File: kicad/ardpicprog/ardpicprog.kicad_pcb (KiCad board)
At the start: 2 copper layers, 69.2 x 53.9 mm, 37 parts, among them P1 CONN_01X06, P2 CONN_01X02, Q1 BC548, SW1 SW_PUSH, U1 PIC16F627, U2 MC34063, U3 LM78L12ACZ

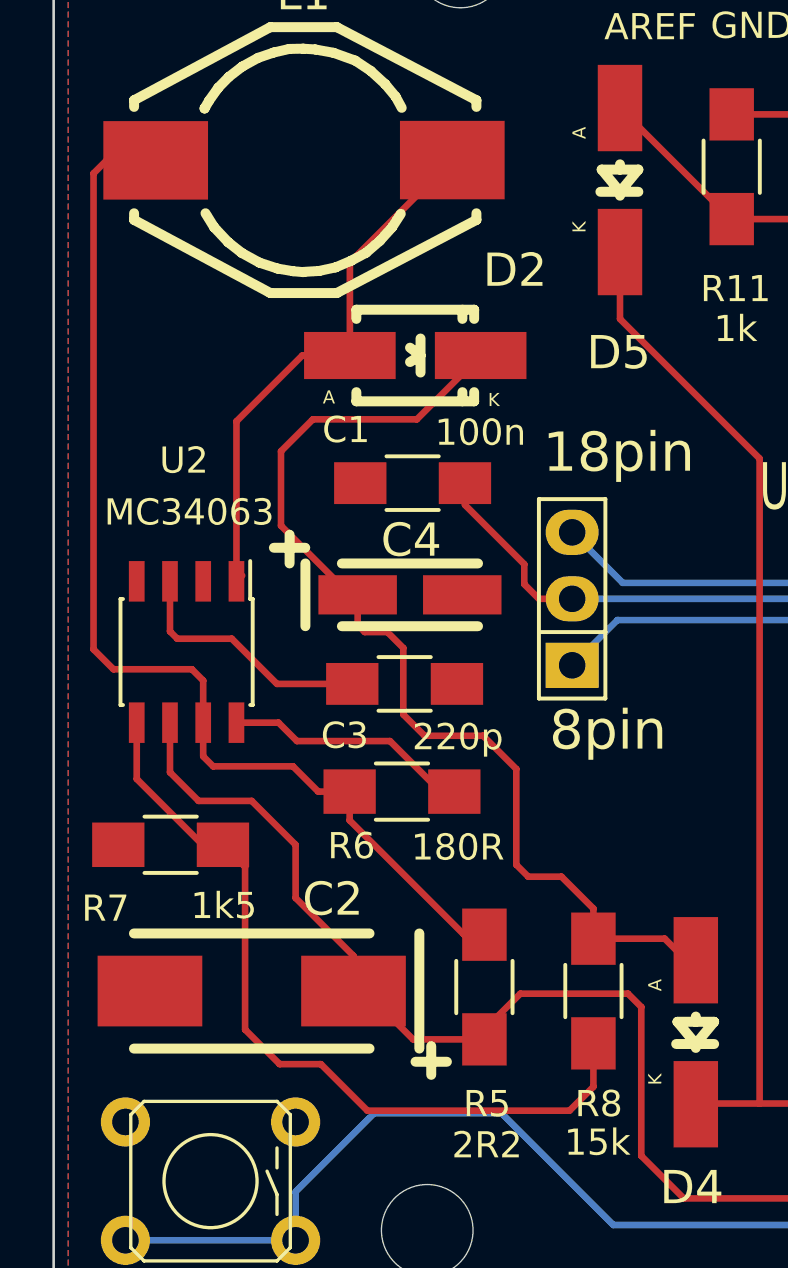
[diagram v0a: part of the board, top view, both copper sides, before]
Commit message: update c2 to 10u/6.3V on 5V line
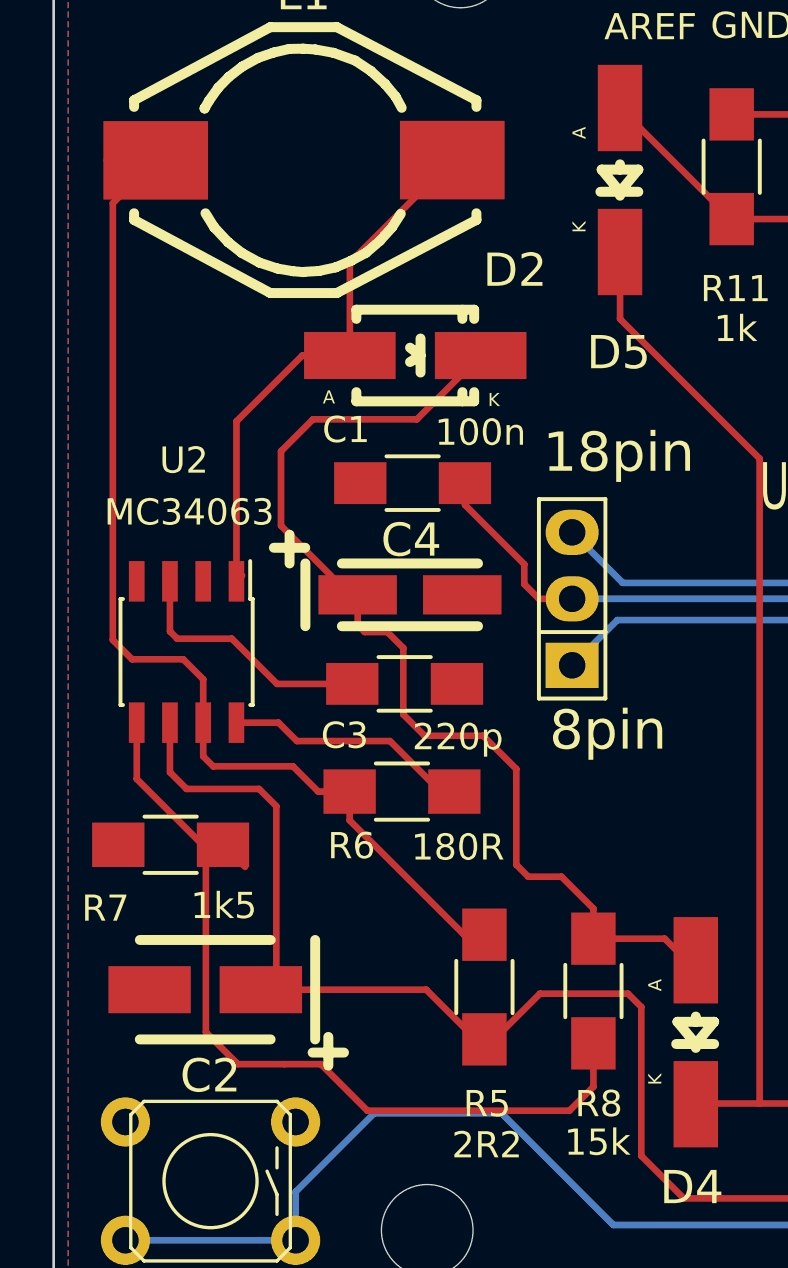
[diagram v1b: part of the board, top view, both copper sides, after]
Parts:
- C2: value 10m/35V -> 10m/6,3V; footprint Capacitors_Tantalum_SMD:TantalC_SizeD_EIA-7343_HandSoldering -> Capacitors_Tantalum_SMD:TantalC_SizeB_EIA-3528_HandSoldering
- moved C2 1.78 mm to (135.1, 118.3)
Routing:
- net 5V: track 51.9 -> 55.0 mm
- net Net-(R7-Pad1): track 30.5 -> 33.2 mm
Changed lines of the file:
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@@
     (links 73)
     (no_connects 0)
-    (area 117.87777 70.9168 221.46623 133.98246)
+    (area 129.286799 76.099199 198.576401 130.148801)
     (thickness 1.6)
     (drawings 34)
-    (tracks 232)
+    (tracks 234)
     (zones 0)
     (modules 37)
@@
       (outputformat 1)
       (mirror false)
-      (drillshape 1)
+      (drillshape 0)
       (scaleselection 1)
       (outputdirectory ""))
@@
     )
   )
-  (module Capacitors_Tantalum_SMD:TantalC_SizeD_EIA-7343_HandSoldering (layer F.Cu)
-    (at 136.906 118.364 180)
-    (descr "Tantal Cap. , Size D, EIA-7343, Hand Soldering,")
-    (tags "Tantal Cap. , Size D, EIA-7343, Hand Soldering,")
-    (attr smd)
-    (fp_text reference C2 (at -3.0988 3.5052 180) (layer F.SilkS)
-      (effects (font (thickness 0.3048)))
-    )
-    (fp_text value 10m/35V (at -0.09906 3.59918 180) (layer F.SilkS) hide
-      (effects (font (thickness 0.3048)))
-    )
-    (fp_line (start -6.40334 -2.19964) (end -6.40334 2.19964) (layer F.SilkS) (width 0.381))
-    (fp_line (start -4.50088 2.19964) (end 4.50088 2.19964) (layer F.SilkS) (width 0.381))
-    (fp_line (start 4.50088 -2.19964) (end -4.50088 -2.19964) (layer F.SilkS) (width 0.381))
-    (fp_text user + (at -6.85546 -2.70002 180) (layer F.SilkS)
-      (effects (font (thickness 0.3048)))
-    )
-    (fp_line (start -6.858 -3.20294) (end -6.858 -2.10312) (layer F.SilkS) (width 0.381))
-    (fp_line (start -7.45744 -2.70256) (end -6.25856 -2.70256) (layer F.SilkS) (width 0.381))
-    (pad 2 smd rect (at 3.88874 0 180) (size 4.0005 2.70002) (layers F.Cu F.Paste F.Mask)
-      (net 2 GND))
-    (pad 1 smd rect (at -3.88874 0 180) (size 4.0005 2.70002) (layers F.Cu F.Paste F.Mask)
-      (net 3 5V))
-  )
   (module Capacitors_SMD:C_1206_HandSoldering (layer F.Cu)
     (at 142.748 106.6292)
@@
     (pad 1 thru_hole circle (at 0 0) (size 3.50012 3.50012) (drill 3.50012) (layers))
   )
+  (module Capacitors_Tantalum_SMD:TantalC_SizeB_EIA-3528_HandSoldering (layer F.Cu)
+    (at 135.128 118.3132 180)
+    (descr "Tantal Cap. , Size B, EIA-3528, Hand Soldering,")
+    (tags "Tantal Cap. , Size B, EIA-3528, Hand Soldering,")
+    (attr smd)
+    (fp_text reference C2 (at -0.20066 -3.29946 180) (layer F.SilkS)
+      (effects (font (thickness 0.3048)))
+    )
+    (fp_text value 10m/6,3V (at -0.09906 3.59918 180) (layer F.SilkS) hide
+      (effects (font (thickness 0.3048)))
+    )
+    (fp_text user + (at -4.70154 -2.4003 180) (layer F.SilkS)
+      (effects (font (thickness 0.3048)))
+    )
+    (fp_line (start -4.20116 -1.89992) (end -4.20116 1.89992) (layer F.SilkS) (width 0.381))
+    (fp_line (start 2.49936 -1.89992) (end -2.49936 -1.89992) (layer F.SilkS) (width 0.381))
+    (fp_line (start 2.49682 1.89992) (end -2.5019 1.89992) (layer F.SilkS) (width 0.381))
+    (fp_line (start -4.70408 -2.90322) (end -4.70408 -1.8034) (layer F.SilkS) (width 0.381))
+    (fp_line (start -5.30352 -2.40284) (end -4.10464 -2.40284) (layer F.SilkS) (width 0.381))
+    (pad 2 smd rect (at 2.12598 0 180) (size 3.1496 1.80086) (layers F.Cu F.Paste F.Mask)
+      (net 2 GND))
+    (pad 1 smd rect (at -2.12598 0 180) (size 3.1496 1.80086) (layers F.Cu F.Paste F.Mask)
+      (net 3 5V))
+  )
   (gr_text AD5 (at 193.3956 125.0188) (layer F.SilkS)
     (effects (font (size 1 1) (thickness 0.15)))
@@
   (segment (start 183.9976 103.378) (end 175.1076 103.378) (width 0.254) (layer B.Cu) (net 1))
   (segment (start 175.1076 103.378) (end 149.1488 103.378) (width 0.254) (layer B.Cu) (net 1))
+  (segment (start 145.796 120.2116) (end 146.1709 120.2116) (width 0.254) (layer F.Cu) (net 3))
+  (segment (start 146.1709 120.2116) (end 147.9169 118.4656) (width 0.254) (layer F.Cu) (net 3))
+  (segment (start 145.796 120.2116) (end 145.4719 120.2116) (width 0.254) (layer F.Cu) (net 3))
+  (segment (start 145.4719 120.2116) (end 143.5735 118.3132) (width 0.254) (layer F.Cu) (net 3))
+  (segment (start 143.5735 118.3132) (end 137.25398 118.3132) (width 0.254) (layer F.Cu) (net 3))
+  (segment (start 134.4168 110.6424) (end 137.1854 110.6424) (width 0.254) (layer F.Cu) (net 3))
+  (segment (start 137.8458 111.3028) (end 137.8458 117.72138) (width 0.254) (layer F.Cu) (net 3))
+  (segment (start 137.1854 110.6424) (end 137.8458 111.3028) (width 0.254) (layer F.Cu) (net 3))
+  (segment (start 137.8458 117.72138) (end 137.25398 118.3132) (width 0.254) (layer F.Cu) (net 3))
   (segment (start 145.796 120.2116) (end 145.796 119.8372) (width 0.254) (layer F.Cu) (net 3))
-  (segment (start 145.796 119.8372) (end 147.1676 118.4656) (width 0.254) (layer F.Cu) (net 3))
   (segment (start 166.624 124.9172) (end 167.7416 126.0348) (width 0.254) (layer F.Cu) (net 3))
   (segment (start 161.544 124.9172) (end 166.624 124.9172) (width 0.254) (layer F.Cu) (net 3))
@@
   (segment (start 151.7904 118.9736) (end 151.7904 124.6632) (width 0.254) (layer F.Cu) (net 3))
   (segment (start 151.2824 118.4656) (end 151.7904 118.9736) (width 0.254) (layer F.Cu) (net 3))
-  (segment (start 147.1676 118.4656) (end 151.2824 118.4656) (width 0.254) (layer F.Cu) (net 3))
+  (segment (start 147.9169 118.4656) (end 151.2824 118.4656) (width 0.254) (layer F.Cu) (net 3))
   (segment (start 167.7416 126.0348) (end 167.7416 127.3048) (width 0.254) (layer F.Cu) (net 3))
-  (segment (start 140.79474 118.364) (end 141.224 118.364) (width 0.254) (layer F.Cu) (net 3))
-  (segment (start 141.224 118.364) (end 143.0716 120.2116) (width 0.254) (layer F.Cu) (net 3))
-  (segment (start 143.0716 120.2116) (end 145.796 120.2116) (width 0.254) (layer F.Cu) (net 3))
   (segment (start 133.7818 108.11) (end 133.7818 110.0074) (width 0.254) (layer F.Cu) (net 3))
-  (segment (start 138.5824 114.808) (end 140.79474 117.02034) (width 0.254) (layer F.Cu) (net 3))
-  (segment (start 138.5824 112.776) (end 138.5824 114.808) (width 0.254) (layer F.Cu) (net 3))
-  (segment (start 136.906 111.0996) (end 138.5824 112.776) (width 0.254) (layer F.Cu) (net 3))
-  (segment (start 134.874 111.0996) (end 136.906 111.0996) (width 0.254) (layer F.Cu) (net 3))
-  (segment (start 133.7818 110.0074) (end 134.874 111.0996) (width 0.254) (layer F.Cu) (net 3))
-  (segment (start 140.79474 117.02034) (end 140.79474 118.364) (width 0.254) (layer F.Cu) (net 3))
+  (segment (start 133.7818 110.0074) (end 134.4168 110.6424) (width 0.254) (layer F.Cu) (net 3))
   (segment (start 140.748 106.6292) (end 137.8712 106.6292) (width 0.254) (layer F.Cu) (net 4))
   (segment (start 133.7818 104.6226) (end 133.7818 102.71) (width 0.254) (layer F.Cu) (net 4))
@@
   (segment (start 170.688 100.6856) (end 170.688 99.4664) (width 0.254) (layer B.Cu) (net 12))
   (segment (start 170.688 100.838) (end 170.688 99.4664) (width 0.254) (layer B.Cu) (net 12))
+  (segment (start 135.0518 108.11) (end 135.0518 106.4514) (width 0.254) (layer F.Cu) (net 13))
+  (segment (start 131.5974 88.26246) (end 133.2357 86.62416) (width 0.254) (layer F.Cu) (net 13))
+  (segment (start 131.5974 104.9528) (end 131.5974 88.26246) (width 0.254) (layer F.Cu) (net 13))
+  (segment (start 132.334 105.6894) (end 131.5974 104.9528) (width 0.254) (layer F.Cu) (net 13))
+  (segment (start 134.2898 105.6894) (end 132.334 105.6894) (width 0.254) (layer F.Cu) (net 13))
+  (segment (start 135.0518 106.4514) (end 134.2898 105.6894) (width 0.254) (layer F.Cu) (net 13))
   (segment (start 133.2357 86.62416) (end 131.35864 86.62416) (width 0.254) (layer F.Cu) (net 13))
-  (segment (start 131.35864 86.62416) (end 130.8608 87.122) (width 0.254) (layer F.Cu) (net 13))
-  (segment (start 130.8608 87.122) (end 130.8608 105.3084) (width 0.254) (layer F.Cu) (net 13))
-  (segment (start 130.8608 105.3084) (end 131.6228 106.0704) (width 0.254) (layer F.Cu) (net 13))
-  (segment (start 131.6228 106.0704) (end 134.62 106.0704) (width 0.254) (layer F.Cu) (net 13))
-  (segment (start 134.62 106.0704) (end 135.0518 106.5022) (width 0.254) (layer F.Cu) (net 13))
-  (segment (start 135.0518 106.5022) (end 135.0518 108.11) (width 0.254) (layer F.Cu) (net 13))
   (segment (start 145.796 116.2116) (end 145.0152 116.2116) (width 0.254) (layer F.Cu) (net 13))
   (segment (start 145.0152 116.2116) (end 140.6464 111.8428) (width 0.254) (layer F.Cu) (net 13))
@@
   (segment (start 137.9296 108.11) (end 138.6332 108.8136) (width 0.254) (layer F.Cu) (net 21))
   (segment (start 144.1196 110.744) (end 144.6464 110.744) (width 0.254) (layer F.Cu) (net 21))
+  (segment (start 138.1506 121.158) (end 136.3726 121.158) (width 0.254) (layer F.Cu) (net 22))
+  (segment (start 135.1534 119.9388) (end 135.1534 113.4298) (width 0.254) (layer F.Cu) (net 22))
+  (segment (start 136.3726 121.158) (end 135.1534 119.9388) (width 0.254) (layer F.Cu) (net 22))
+  (segment (start 135.1534 113.4298) (end 135.8072 112.776) (width 0.254) (layer F.Cu) (net 22))
   (segment (start 149.9616 120.364) (end 149.9616 122.0216) (width 0.254) (layer F.Cu) (net 22))
-  (segment (start 136.652 119.8372) (end 136.652 113.6208) (width 0.254) (layer F.Cu) (net 22))
-  (segment (start 137.9728 121.158) (end 136.652 119.8372) (width 0.254) (layer F.Cu) (net 22))
-  (segment (start 139.5476 121.158) (end 137.9728 121.158) (width 0.254) (layer F.Cu) (net 22))
+  (segment (start 139.5476 121.158) (end 138.1506 121.158) (width 0.254) (layer F.Cu) (net 22))
   (segment (start 141.3256 122.936) (end 139.5476 121.158) (width 0.254) (layer F.Cu) (net 22))
   (segment (start 149.0472 122.936) (end 141.3256 122.936) (width 0.254) (layer F.Cu) (net 22))
